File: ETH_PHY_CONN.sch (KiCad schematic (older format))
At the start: 13 parts

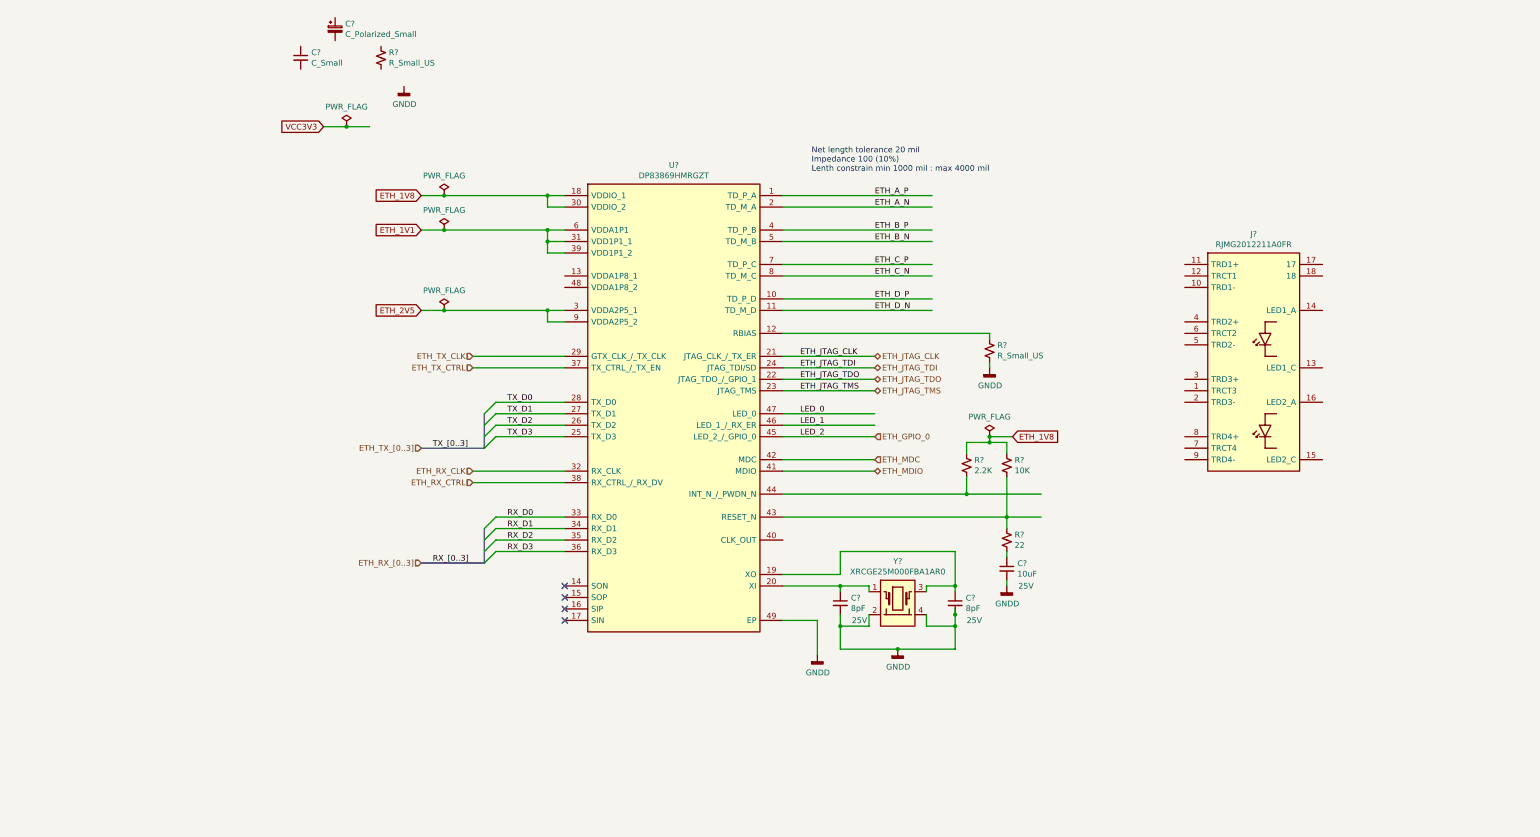
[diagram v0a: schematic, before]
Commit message: Added USB SRAM sheet,Added USB3 ethernet ic
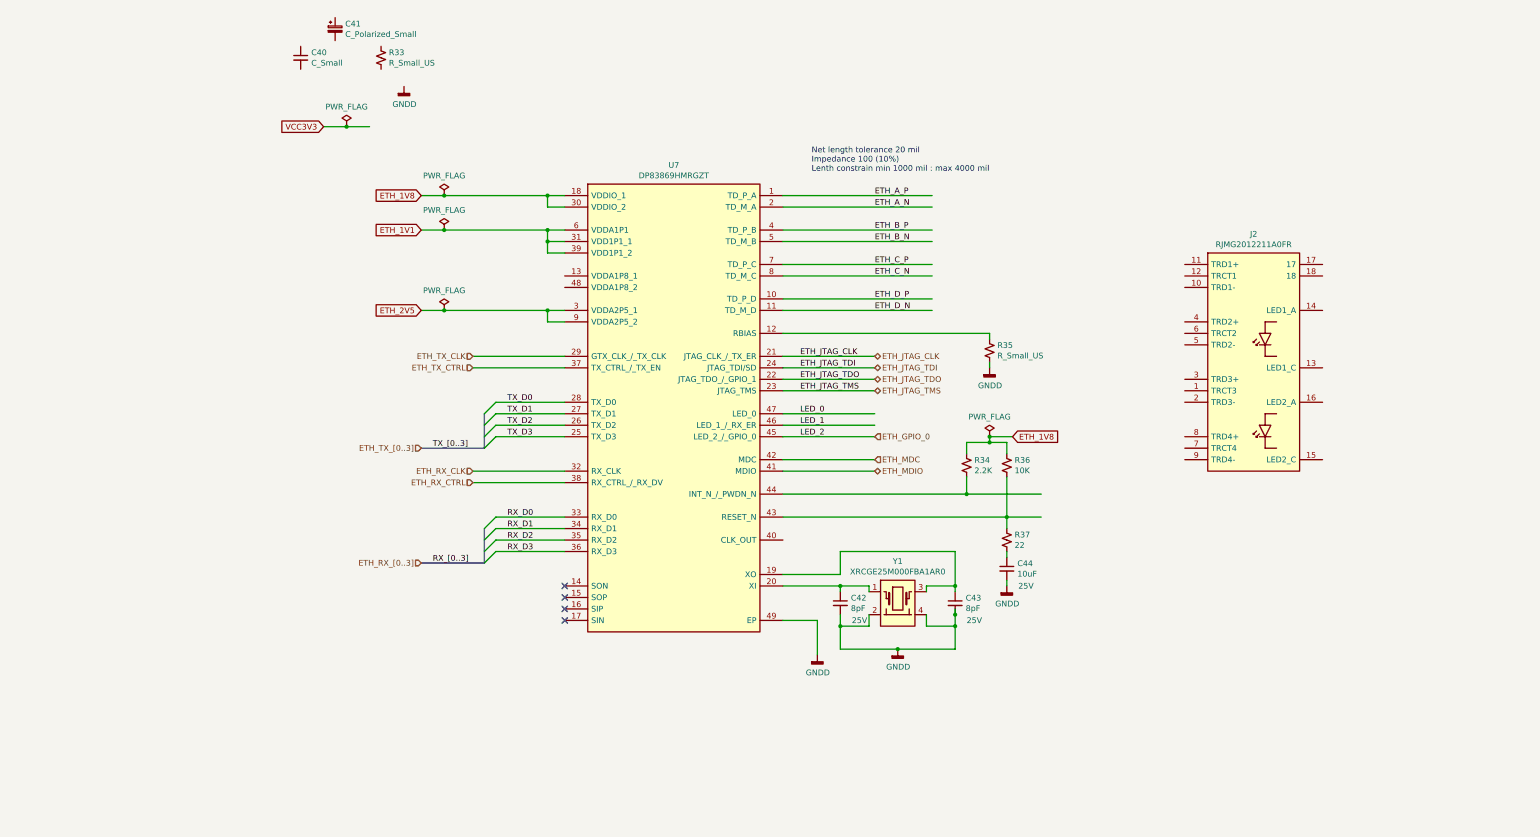
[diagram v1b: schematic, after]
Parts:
- gave numbers to parts that had none: 13
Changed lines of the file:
@@
 $Descr A4 11693 8268
 encoding utf-8
-Sheet 12 15
+Sheet 12 17
 Title ""
 Date ""
@@
 P 8700 2650
 AR Path="/601E7C92/6026D902" Ref="J?"  Part="1"
-AR Path="/601E7C92/60257FE5/6026D902" Ref="J?"  Part="1"
-F 0 "J?" H 9100 2815 50  0000 C CNN
+AR Path="/601E7C92/60257FE5/6026D902" Ref="J2"  Part="1"
+F 0 "J2" H 9100 2815 50  0000 C CNN
 F 1 "RJMG2012211A0FR" H 9100 2724 50  0000 C CNN
 F 2 "Connector_RJ:RJ45_Amphenol_RJMG2012211A0FR" H 10450 2350 50  0001 L CNN
@@
 P 3300 2050
 AR Path="/601E7C92/6026D908" Ref="U?"  Part="1"
-AR Path="/601E7C92/60257FE5/6026D908" Ref="U?"  Part="1"
-F 0 "U?" H 4050 2215 50  0000 C CNN
+AR Path="/601E7C92/60257FE5/6026D908" Ref="U7"  Part="1"
+F 0 "U7" H 4050 2215 50  0000 C CNN
 F 1 "DP83869HMRGZT" H 4050 2124 50  0000 C CNN
 F 2 "QFN50P700X700X100-49N-D" H 6850 1150 50  0001 L CNN
@@
 AR Path="/601E7CC8/6026D90E" Ref="R?"  Part="1"
 AR Path="/601E7C92/6026D90E" Ref="R?"  Part="1"
-AR Path="/601E7C92/60257FE5/6026D90E" Ref="R?"  Part="1"
-F 0 "R?" H 1568 996 50  0000 L CNN
+AR Path="/601E7C92/60257FE5/6026D90E" Ref="R33"  Part="1"
+F 0 "R33" H 1568 996 50  0000 L CNN
 F 1 "R_Small_US" H 1568 905 50  0000 L CNN
 F 2 "Resistor_SMD:R_0603_1608Metric_Pad0.98x0.95mm_HandSolder" H 1500 950 50  0001 C CNN
@@
 AR Path="/601E7CC8/6026D915" Ref="C?"  Part="1"
 AR Path="/601E7C92/6026D915" Ref="C?"  Part="1"
-AR Path="/601E7C92/60257FE5/6026D915" Ref="C?"  Part="1"
-F 0 "C?" H 892 996 50  0000 L CNN
+AR Path="/601E7C92/60257FE5/6026D915" Ref="C40"  Part="1"
+F 0 "C40" H 892 996 50  0000 L CNN
 F 1 "C_Small" H 892 905 50  0000 L CNN
 F 2 "Capacitor_SMD:C_0603_1608Metric_Pad1.08x0.95mm_HandSolder" H 800 950 50  0001 C CNN
@@
 AR Path="/601E7CC8/6026D91C" Ref="#FLG?"  Part="1"
 AR Path="/601E7C92/6026D91C" Ref="#FLG?"  Part="1"
-AR Path="/601E7C92/60257FE5/6026D91C" Ref="#FLG?"  Part="1"
-F 0 "#FLG?" H 1200 1625 50  0001 C CNN
+AR Path="/601E7C92/60257FE5/6026D91C" Ref="#FLG011"  Part="1"
+F 0 "#FLG011" H 1200 1625 50  0001 C CNN
 F 1 "PWR_FLAG" H 1200 1723 50  0000 C CNN
 F 2 "" H 1200 1550 50  0001 C CNN
@@
 AR Path="/601E7CC8/6026D925" Ref="#PWR?"  Part="1"
 AR Path="/601E7C92/6026D925" Ref="#PWR?"  Part="1"
-AR Path="/601E7C92/60257FE5/6026D925" Ref="#PWR?"  Part="1"
-F 0 "#PWR?" H 1700 950 50  0001 C CNN
+AR Path="/601E7C92/60257FE5/6026D925" Ref="#PWR05"  Part="1"
+F 0 "#PWR05" H 1700 950 50  0001 C CNN
 F 1 "GNDD" H 1704 1045 50  0000 C CNN
 F 2 "" H 1700 1200 50  0001 C CNN
@@
 P 1100 700
 AR Path="/601E7C92/6026D92C" Ref="C?"  Part="1"
-AR Path="/601E7C92/60257FE5/6026D92C" Ref="C?"  Part="1"
-F 0 "C?" H 1188 746 50  0000 L CNN
+AR Path="/601E7C92/60257FE5/6026D92C" Ref="C41"  Part="1"
+F 0 "C41" H 1188 746 50  0000 L CNN
 F 1 "C_Polarized_Small" H 1188 655 50  0000 L CNN
 F 2 "Capacitor_Tantalum_SMD:CP_EIA-1608-10_AVX-L_Pad1.25x1.05mm_HandSolder" H 1100 700 50  0001 C CNN
@@
 AR Path="/601E7CC8/6026D933" Ref="#FLG?"  Part="1"
 AR Path="/601E7C92/6026D933" Ref="#FLG?"  Part="1"
-AR Path="/601E7C92/60257FE5/6026D933" Ref="#FLG?"  Part="1"
-F 0 "#FLG?" H 2050 2225 50  0001 C CNN
+AR Path="/601E7C92/60257FE5/6026D933" Ref="#FLG012"  Part="1"
+F 0 "#FLG012" H 2050 2225 50  0001 C CNN
 F 1 "PWR_FLAG" H 2050 2323 50  0000 C CNN
 F 2 "" H 2050 2150 50  0001 C CNN
@@
 AR Path="/601E7CC8/6026D93C" Ref="#FLG?"  Part="1"
 AR Path="/601E7C92/6026D93C" Ref="#FLG?"  Part="1"
-AR Path="/601E7C92/60257FE5/6026D93C" Ref="#FLG?"  Part="1"
-F 0 "#FLG?" H 2050 2525 50  0001 C CNN
+AR Path="/601E7C92/60257FE5/6026D93C" Ref="#FLG013"  Part="1"
+F 0 "#FLG013" H 2050 2525 50  0001 C CNN
 F 1 "PWR_FLAG" H 2050 2623 50  0000 C CNN
 F 2 "" H 2050 2450 50  0001 C CNN
@@
 AR Path="/601E7CC8/6026D945" Ref="#FLG?"  Part="1"
 AR Path="/601E7C92/6026D945" Ref="#FLG?"  Part="1"
-AR Path="/601E7C92/60257FE5/6026D945" Ref="#FLG?"  Part="1"
-F 0 "#FLG?" H 2050 3225 50  0001 C CNN
+AR Path="/601E7C92/60257FE5/6026D945" Ref="#FLG014"  Part="1"
+F 0 "#FLG014" H 2050 3225 50  0001 C CNN
 F 1 "PWR_FLAG" H 2050 3323 50  0000 C CNN
 F 2 "" H 2050 3150 50  0001 C CNN
@@
 AR Path="/601E7CC8/6026D99A" Ref="R?"  Part="1"
 AR Path="/601E7C92/6026D99A" Ref="R?"  Part="1"
-AR Path="/601E7C92/60257FE5/6026D99A" Ref="R?"  Part="1"
-F 0 "R?" H 6868 3546 50  0000 L CNN
+AR Path="/601E7C92/60257FE5/6026D99A" Ref="R35"  Part="1"
+F 0 "R35" H 6868 3546 50  0000 L CNN
 F 1 "R_Small_US" H 6868 3455 50  0000 L CNN
 F 2 "Resistor_SMD:R_0603_1608Metric_Pad0.98x0.95mm_HandSolder" H 6800 3500 50  0001 C CNN
@@
 AR Path="/601E7CC8/6026D9A1" Ref="#PWR?"  Part="1"
 AR Path="/601E7C92/6026D9A1" Ref="#PWR?"  Part="1"
-AR Path="/601E7C92/60257FE5/6026D9A1" Ref="#PWR?"  Part="1"
-F 0 "#PWR?" H 6800 3400 50  0001 C CNN
+AR Path="/601E7C92/60257FE5/6026D9A1" Ref="#PWR026"  Part="1"
+F 0 "#PWR026" H 6800 3400 50  0001 C CNN
 F 1 "GNDD" H 6804 3495 50  0000 C CNN
 F 2 "" H 6800 3650 50  0001 C CNN
@@
 AR Path="/601E7CC8/6026D9C4" Ref="#FLG?"  Part="1"
 AR Path="/601E7C92/6026D9C4" Ref="#FLG?"  Part="1"
-AR Path="/601E7C92/60257FE5/6026D9C4" Ref="#FLG?"  Part="1"
-F 0 "#FLG?" H 6800 4325 50  0001 C CNN
+AR Path="/601E7C92/60257FE5/6026D9C4" Ref="#FLG015"  Part="1"
+F 0 "#FLG015" H 6800 4325 50  0001 C CNN
 F 1 "PWR_FLAG" H 6800 4423 50  0000 C CNN
 F 2 "" H 6800 4250 50  0001 C CNN
@@
 AR Path="/601E7CC8/6026D9CB" Ref="R?"  Part="1"
 AR Path="/601E7C92/6026D9CB" Ref="R?"  Part="1"
-AR Path="/601E7C92/60257FE5/6026D9CB" Ref="R?"  Part="1"
-F 0 "R?" H 6668 4546 50  0000 L CNN
+AR Path="/601E7C92/60257FE5/6026D9CB" Ref="R34"  Part="1"
+F 0 "R34" H 6668 4546 50  0000 L CNN
 F 1 "2.2K" H 6668 4455 50  0000 L CNN
 F 2 "Resistor_SMD:R_0603_1608Metric_Pad0.98x0.95mm_HandSolder" H 6600 4500 50  0001 C CNN
@@
 AR Path="/601E7CC8/6026D9D1" Ref="R?"  Part="1"
 AR Path="/601E7C92/6026D9D1" Ref="R?"  Part="1"
-AR Path="/601E7C92/60257FE5/6026D9D1" Ref="R?"  Part="1"
-F 0 "R?" H 7018 4546 50  0000 L CNN
+AR Path="/601E7C92/60257FE5/6026D9D1" Ref="R36"  Part="1"
+F 0 "R36" H 7018 4546 50  0000 L CNN
 F 1 "10K" H 7018 4455 50  0000 L CNN
 F 2 "Resistor_SMD:R_0603_1608Metric_Pad0.98x0.95mm_HandSolder" H 6950 4500 50  0001 C CNN
@@
 AR Path="/601E7CC8/6026D9E5" Ref="R?"  Part="1"
 AR Path="/601E7C92/6026D9E5" Ref="R?"  Part="1"
-AR Path="/601E7C92/60257FE5/6026D9E5" Ref="R?"  Part="1"
-F 0 "R?" H 7018 5196 50  0000 L CNN
+AR Path="/601E7C92/60257FE5/6026D9E5" Ref="R37"  Part="1"
+F 0 "R37" H 7018 5196 50  0000 L CNN
 F 1 "22" H 7018 5105 50  0000 L CNN
 F 2 "Resistor_SMD:R_0603_1608Metric_Pad0.98x0.95mm_HandSolder" H 6950 5150 50  0001 C CNN
@@
 AR Path="/601E7CC8/6026D9EC" Ref="C?"  Part="1"
 AR Path="/601E7C92/6026D9EC" Ref="C?"  Part="1"
-AR Path="/601E7C92/60257FE5/6026D9EC" Ref="C?"  Part="1"
-F 0 "C?" H 7042 5446 50  0000 L CNN
+AR Path="/601E7C92/60257FE5/6026D9EC" Ref="C44"  Part="1"
+F 0 "C44" H 7042 5446 50  0000 L CNN
 F 1 "10uF" H 7042 5355 50  0000 L CNN
 F 2 "Capacitor_SMD:C_0603_1608Metric_Pad1.08x0.95mm_HandSolder" H 6950 5400 50  0001 C CNN
@@
 AR Path="/601E7CC8/6026D9F2" Ref="#PWR?"  Part="1"
 AR Path="/601E7C92/6026D9F2" Ref="#PWR?"  Part="1"
-AR Path="/601E7C92/60257FE5/6026D9F2" Ref="#PWR?"  Part="1"
-F 0 "#PWR?" H 6950 5300 50  0001 C CNN
+AR Path="/601E7C92/60257FE5/6026D9F2" Ref="#PWR027"  Part="1"
+F 0 "#PWR027" H 6950 5300 50  0001 C CNN
 F 1 "GNDD" H 6954 5395 50  0000 C CNN
 F 2 "" H 6950 5550 50  0001 C CNN
@@
 	6950 5500 6950 5550
 $Comp
-L GM_Crystals_Oscilators_n_Resonators:XRCGE25M000FBA1AR0 Y?
+L GM_Crystals_Oscilators_n_Resonators:XRCGE25M000FBA1AR0 Y1
 U 1 1 60287815
 P 5850 5500
-F 0 "Y?" H 6000 5665 50  0000 C CNN
+F 0 "Y1" H 6000 5665 50  0000 C CNN
 F 1 "XRCGE25M000FBA1AR0" H 6000 5574 50  0000 C CNN
 F 2 "GM_Crystals_Oscilators_n_Resonators:XRCGE25M000FBA1AR0" H 7360 5830 50  0001 C CNN
@@
 AR Path="/601E7CC8/6028F5F9" Ref="C?"  Part="1"
 AR Path="/601E7C92/6028F5F9" Ref="C?"  Part="1"
-AR Path="/601E7C92/60257FE5/6028F5F9" Ref="C?"  Part="1"
-F 0 "C?" H 5592 5746 50  0000 L CNN
+AR Path="/601E7C92/60257FE5/6028F5F9" Ref="C42"  Part="1"
+F 0 "C42" H 5592 5746 50  0000 L CNN
 F 1 "8pF" H 5592 5655 50  0000 L CNN
 F 2 "Capacitor_SMD:C_0603_1608Metric_Pad1.08x0.95mm_HandSolder" H 5500 5700 50  0001 C CNN
@@
 AR Path="/601E7CC8/602910D2" Ref="C?"  Part="1"
 AR Path="/601E7C92/602910D2" Ref="C?"  Part="1"
-AR Path="/601E7C92/60257FE5/602910D2" Ref="C?"  Part="1"
-F 0 "C?" H 6592 5746 50  0000 L CNN
+AR Path="/601E7C92/60257FE5/602910D2" Ref="C43"  Part="1"
+F 0 "C43" H 6592 5746 50  0000 L CNN
 F 1 "8pF" H 6592 5655 50  0000 L CNN
 F 2 "Capacitor_SMD:C_0603_1608Metric_Pad1.08x0.95mm_HandSolder" H 6500 5700 50  0001 C CNN
@@
 AR Path="/601E7CC8/602ACCE3" Ref="#PWR?"  Part="1"
 AR Path="/601E7C92/602ACCE3" Ref="#PWR?"  Part="1"
-AR Path="/601E7C92/60257FE5/602ACCE3" Ref="#PWR?"  Part="1"
-F 0 "#PWR?" H 6000 5850 50  0001 C CNN
+AR Path="/601E7C92/60257FE5/602ACCE3" Ref="#PWR025"  Part="1"
+F 0 "#PWR025" H 6000 5850 50  0001 C CNN
 F 1 "GNDD" H 6004 5945 50  0000 C CNN
 F 2 "" H 6000 6100 50  0001 C CNN
@@
 AR Path="/601E7CC8/602BD0E2" Ref="#PWR?"  Part="1"
 AR Path="/601E7C92/602BD0E2" Ref="#PWR?"  Part="1"
-AR Path="/601E7C92/60257FE5/602BD0E2" Ref="#PWR?"  Part="1"
-F 0 "#PWR?" H 5300 5900 50  0001 C CNN
+AR Path="/601E7C92/60257FE5/602BD0E2" Ref="#PWR024"  Part="1"
+F 0 "#PWR024" H 5300 5900 50  0001 C CNN
 F 1 "GNDD" H 5304 5995 50  0000 C CNN
 F 2 "" H 5300 6150 50  0001 C CNN

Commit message: Drawn Ethernet PHY schematic (continue...)
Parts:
- added C? (x17): 0.1uF, Capacitor_SMD:C_0603_1608Metric_Pad1.08x0.95mm_HandSolder, symbol Device:C_Small
- added C? (x7): 1uF, Capacitor_SMD:C_0603_1608Metric_Pad1.08x0.95mm_HandSolder, symbol Device:C_Small
- added IC?: SN74LVC3G14DCUR, SOP50P310X90-8N, symbol GM_Gates_n_Inverters:SN74LVC3G14DCUR
- added IC? (x2): TPD4E05U06QDQARQ1, DQA(R-PUSON-N10), symbol GM_Protection:TPD4E05U06QDQARQ1
- added R? (x3): 0, Resistor_SMD:R_0603_1608Metric_Pad0.98x0.95mm_HandSolder, symbol Device:R_Small_US
- added R? (x3): 330, Resistor_SMD:R_0603_1608Metric_Pad0.98x0.95mm_HandSolder, symbol Device:R_Small_US
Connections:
- net labels added: LED_P_0, LED_P_1, LED_P_2, VCC5V
- wire segments 90 -> 231
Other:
- note added: "LED\nSML-P13PTT86R"
- moved on the sheet: C40, C41, C42, C43, C44, J2, R33, R34, R35, R36, R37, U7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
